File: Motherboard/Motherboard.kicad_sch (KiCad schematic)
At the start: 61 parts, among them J1 ATX-20, J2 65SIB_Connector, J3 DB9_Header, J4 GPIO_Connector, J5 Expansion_Connector, J6 Expansion_Connector, J7 Expansion_Connector, J8 Expansion_Connector, J9 Expansion_Connector, SW1 SW_SPST, U2 AS6C4008-55PCN, U3 ATF22V10C, U4 DS1813, U6 28C010, X1 ACO-8MHz

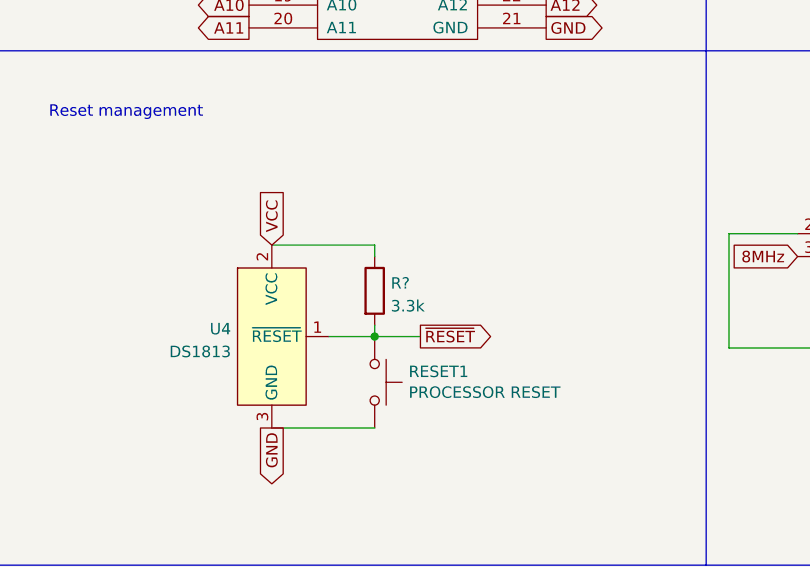
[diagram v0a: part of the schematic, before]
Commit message: 6 unrouted traces...
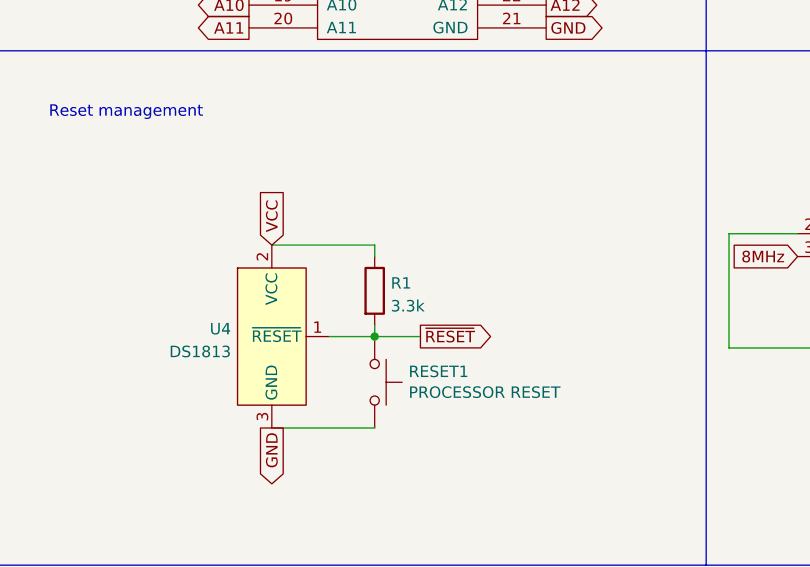
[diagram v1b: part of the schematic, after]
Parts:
- gave numbers to parts that had none: 1
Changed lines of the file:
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@@
   (symbol (lib_id "Device:R") (at 104.14 208.28 0) (unit 1)
     (in_bom yes) (on_board yes) (fields_autoplaced)
-    (property "Reference" "R?" (id 0) (at 105.918 207.4453 0)
+    (property "Reference" "R1" (id 0) (at 105.918 207.4453 0)
       (effects (font (size 1.27 1.27)) (justify left))
     )
@@
       (reference "PWR_OK1") (unit 1) (value "LED") (footprint "LED_THT:LED_D5.0mm")
     )
+    (path "/dde2964d-78c7-464b-aee8-feca4368665c"
+      (reference "R1") (unit 1) (value "3.3k") (footprint "")
+    )
     (path "/dcd42140-1abc-4c79-b38e-d454cf8ccfb6"
       (reference "R9") (unit 1) (value "220 Ω") (footprint "Resistor_THT:R_Axial_DIN0207_L6.3mm_D2.5mm_P7.62mm_Horizontal")
@@
       (reference "R21") (unit 1) (value "3.3k Ω") (footprint "Resistor_THT:R_Axial_DIN0207_L6.3mm_D2.5mm_P7.62mm_Horizontal")
     )
-    (path "/dde2964d-78c7-464b-aee8-feca4368665c"
-      (reference "R?") (unit 1) (value "3.3k") (footprint "")
-    )
     (path "/00000000-0000-0000-0000-00006196bac3"

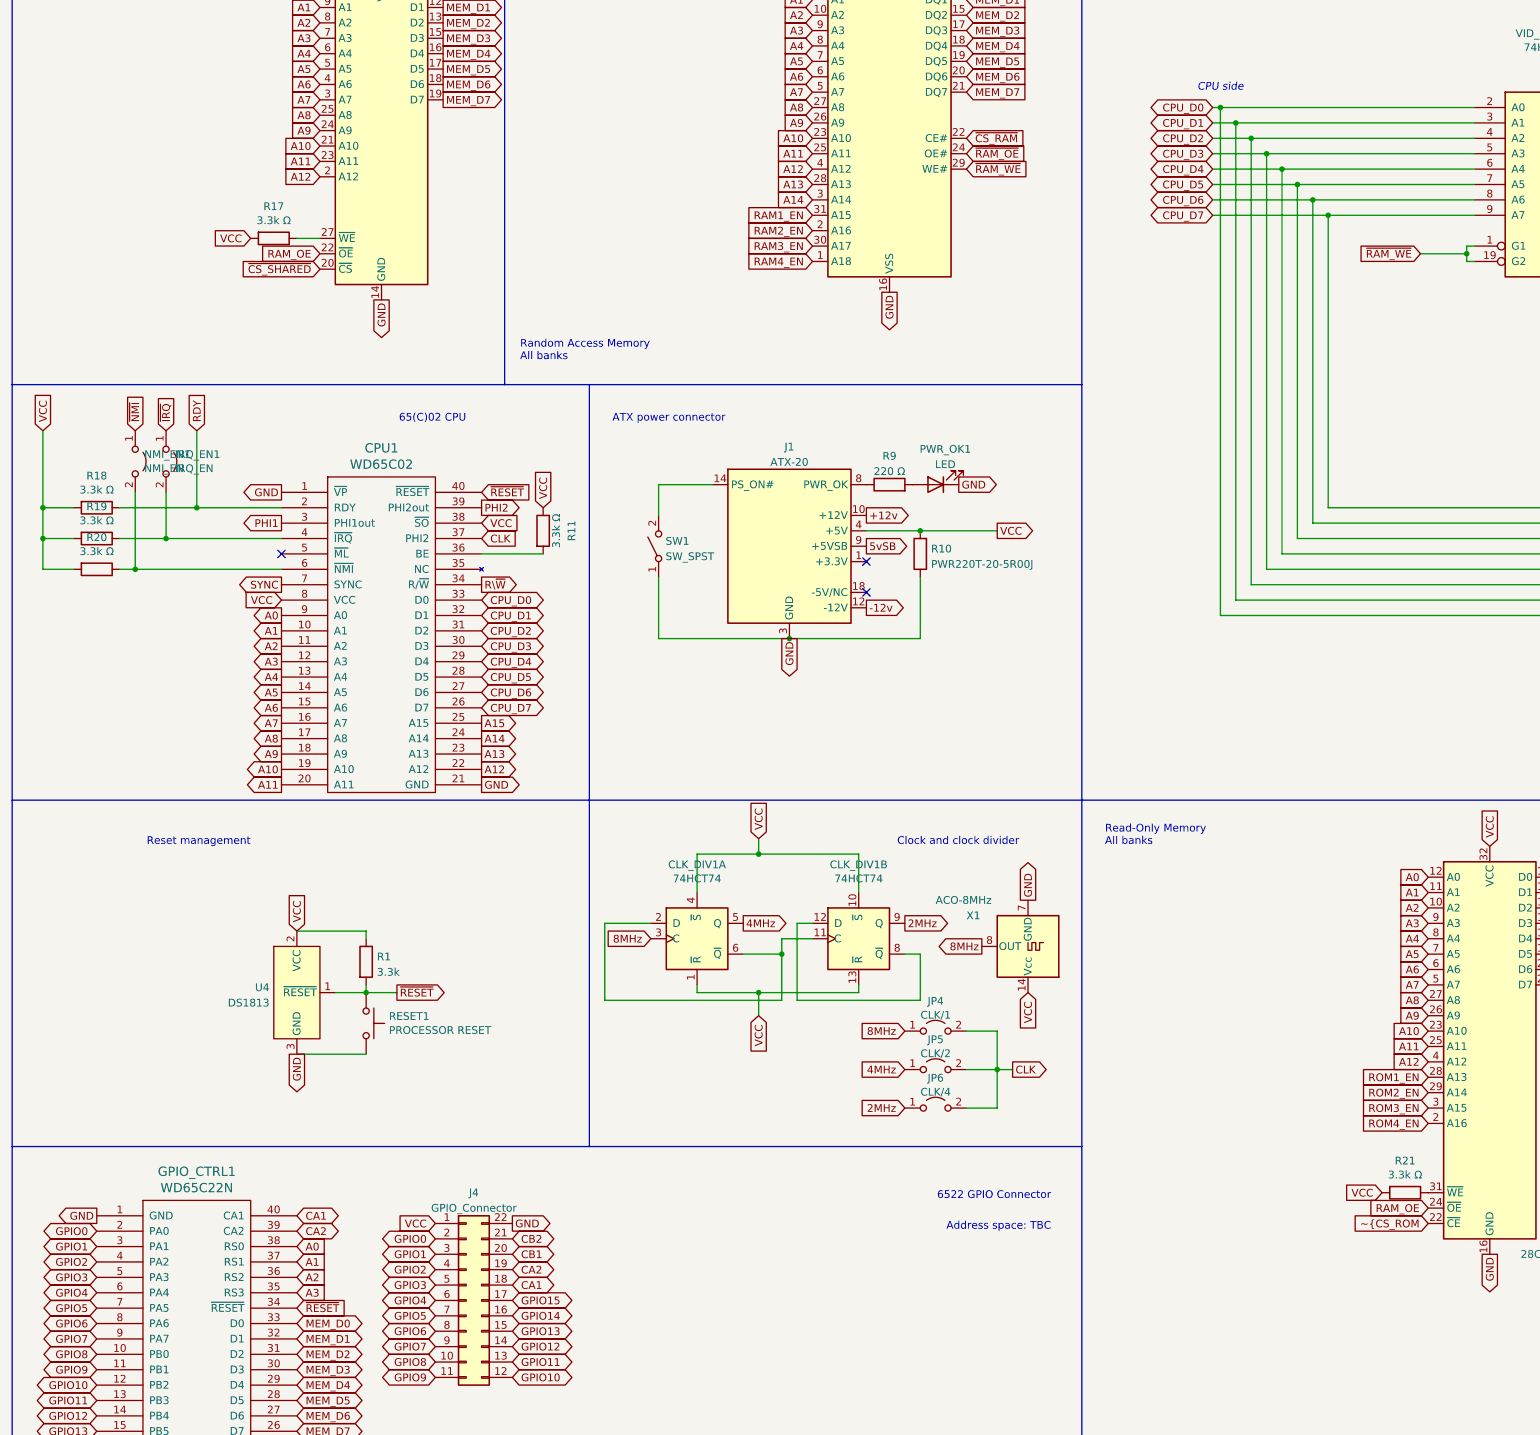
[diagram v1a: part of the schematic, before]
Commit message: Update Motherboard.kicad_sch
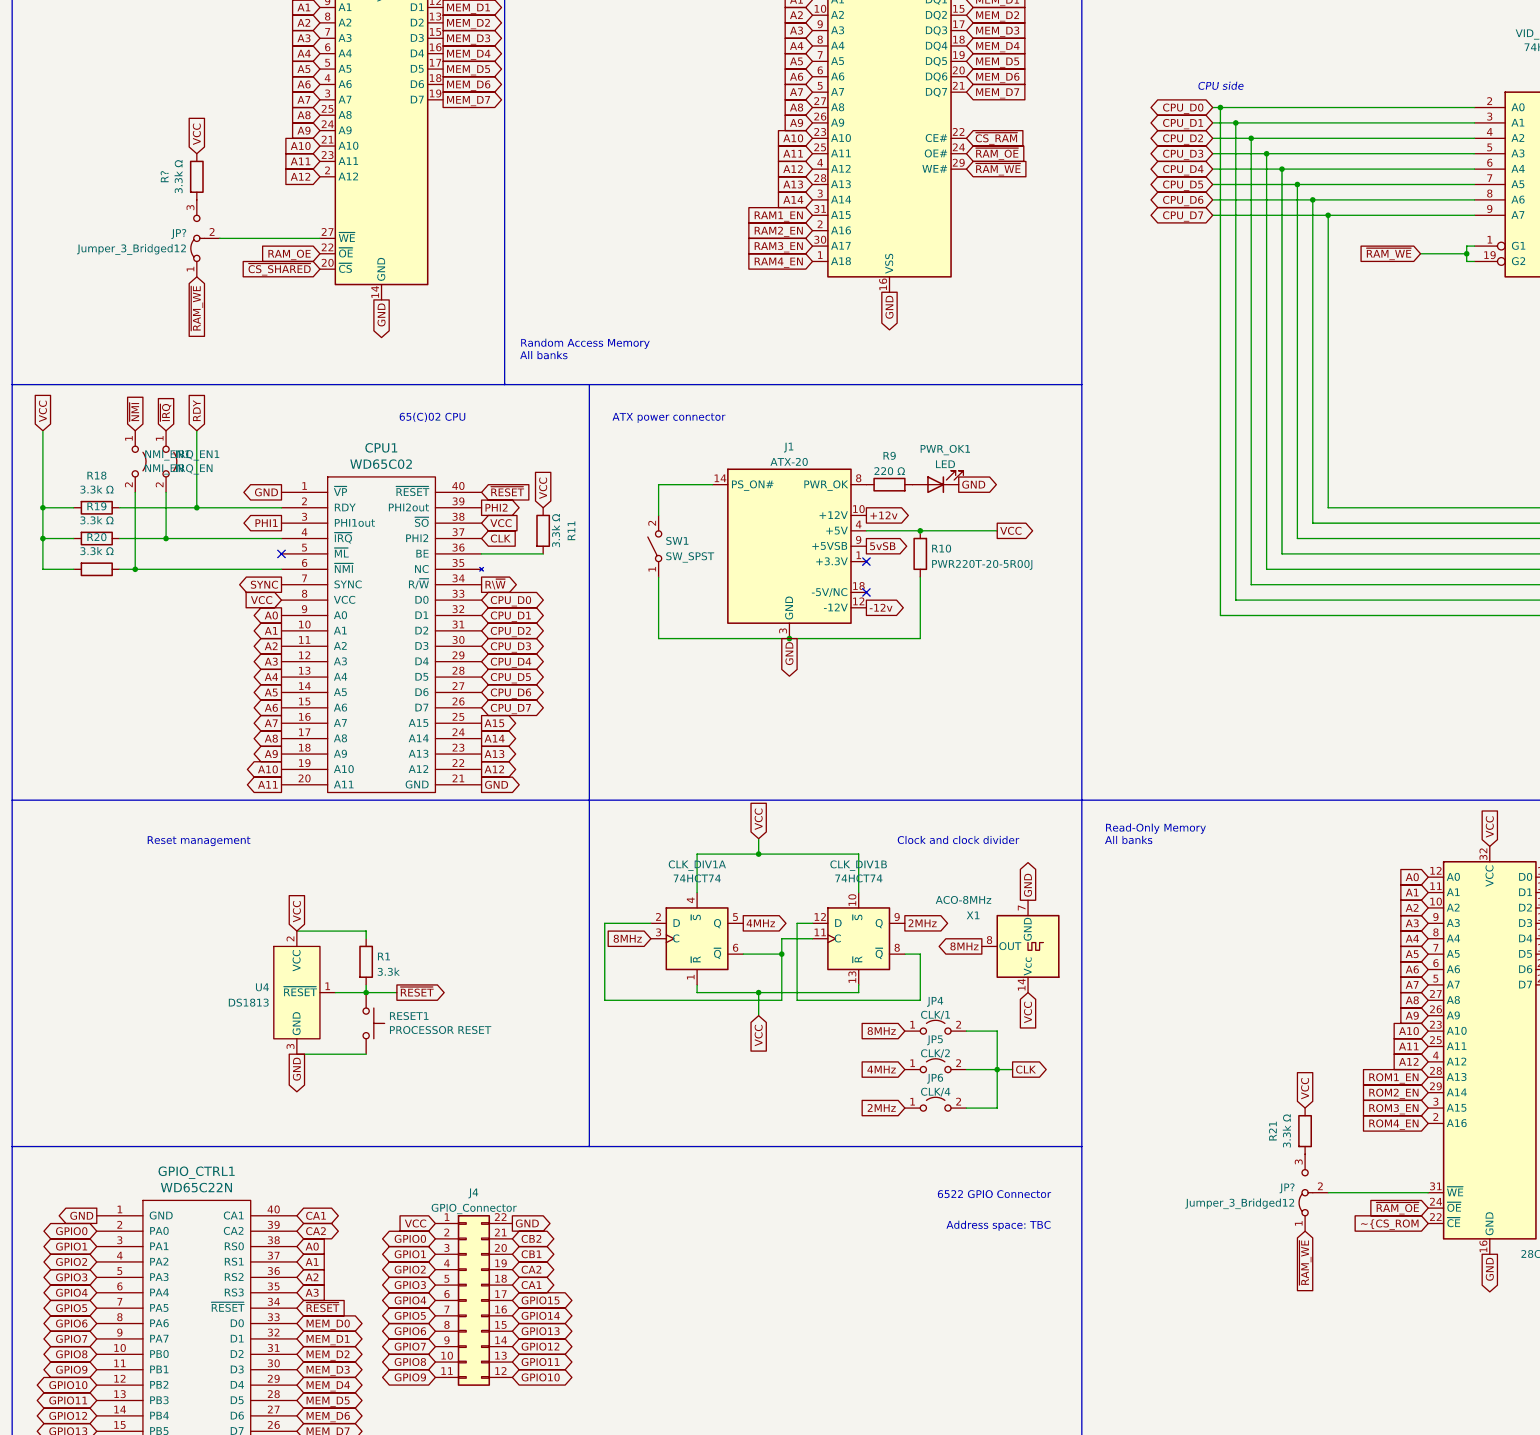
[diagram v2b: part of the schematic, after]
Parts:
- removed R17: 3.3k Ω, Resistor_THT:R_Axial_DIN0207_L6.3mm_D2.5mm_P7.62mm_Horizontal, symbol Device:R
- added JP? (x2): Jumper_3_Bridged12, symbol Jumper:Jumper_3_Bridged12
- added R?: 3.3k Ω, Resistor_THT:R_Axial_DIN0207_L6.3mm_D2.5mm_P7.62mm_Horizontal, symbol Device:R
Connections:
- net RAM_OE: no longer U6.24 (~{OE})
- net VCC: now also R21.1, R?.1; no longer R21.2
- net ~{RAM_OE}: now also U6.24 (~{OE})
- net ~{RAM_WE}: now also JP?.1 (A), JP?.1 (A)
- net at SHARED_ROM1.27 (~{WE}): now also JP?.2 (C)
- net at U6.31 (~{WE}): now also JP?.2 (C); no longer R21.1
- new net: JP?.3 (B), R21.2
- new net: JP?.3 (B), R?.2
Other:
- moved on the sheet: R21
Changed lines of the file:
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@@
     (stroke (width 0) (type default) (color 0 0 0 0))
   )
+  (wire (pts (xy 80.01 88.9) (xy 96.52 88.9))
+    (stroke (width 0) (type default) (color 0 0 0 0))
+  )
   (wire (pts (xy 349.25 72.39) (xy 355.6 72.39))
     (stroke (width 0) (type default) (color 0 0 0 0))
@@
     (stroke (width 0) (type default) (color 0 0 0 0))
   )
-  (wire (pts (xy 92.71 88.9) (xy 96.52 88.9))
-    (stroke (width 0) (type default) (color 0 0 0 0))
-  )
   (wire (pts (xy 158.75 190.5) (xy 168.91 190.5))
     (stroke (width 0) (type default) (color 0 0 0 0))
@@
     (stroke (width 0) (type default) (color 0 0 0 0))
   )
+  (wire (pts (xy 262.89 246.38) (xy 279.4 246.38))
+    (stroke (width 0) (type default) (color 0 0 0 0))
+  )
   (wire (pts (xy 243.84 72.39) (xy 250.19 72.39))
     (stroke (width 0) (type default) (color 0 0 0 0))
@@
     )
   )
+  (global_label "~{RAM_WE}" (shape input) (at 76.2 95.25 270) (fields_autoplaced)
+    (effects (font (size 1.27 1.27)) (justify right))
+    (property "Intersheet References" "${INTERSHEET_REFS}" (id 0) (at 76.1206 104.9523 90)
+      (effects (font (size 1.27 1.27)) (justify right) hide)
+    )
+  )
   (global_label "MEM_D2" (shape output) (at 116.84 53.34 0) (fields_autoplaced)
     (effects (font (size 1.27 1.27)) (justify left))
@@
     )
   )
+  (global_label "VCC" (shape input) (at 76.2 74.93 90) (fields_autoplaced)
+    (effects (font (size 1.27 1.27)) (justify left))
+    (property "Intersheet References" "${INTERSHEET_REFS}" (id 0) (at 311.15 -190.5 0)
+      (effects (font (size 1.27 1.27)) hide)
+    )
+  )
   (global_label "A11" (shape input) (at 751.84 322.58 180) (fields_autoplaced)
     (effects (font (size 1.27 1.27)) (justify right))
@@
     )
   )
-  (global_label "VCC" (shape input) (at 85.09 88.9 180) (fields_autoplaced)
-    (effects (font (size 1.27 1.27)) (justify right))
-    (property "Intersheet References" "${INTERSHEET_REFS}" (id 0) (at 0 0 0)
-      (effects (font (size 1.27 1.27)) hide)
-    )
-  )
   (global_label "~{RAM_OE}" (shape input) (at 203.2 74.93 0) (fields_autoplaced)
     (effects (font (size 1.27 1.27)) (justify left))
@@
     )
   )
+  (global_label "~{RAM_WE}" (shape input) (at 259.08 252.73 270) (fields_autoplaced)
+    (effects (font (size 1.27 1.27)) (justify right))
+    (property "Intersheet References" "${INTERSHEET_REFS}" (id 0) (at 259.0006 262.4323 90)
+      (effects (font (size 1.27 1.27)) (justify right) hide)
+    )
+  )
   (global_label "GPIO11" (shape bidirectional) (at 59.69 280.67 180) (fields_autoplaced)
     (effects (font (size 1.27 1.27)) (justify right))
@@
     )
   )
-  (global_label "RAM_OE" (shape input) (at 279.4 248.92 180) (fields_autoplaced)
+  (global_label "~{RAM_OE}" (shape input) (at 279.4 248.92 180) (fields_autoplaced)
     (effects (font (size 1.27 1.27)) (justify right))
     (property "Intersheet References" "${INTERSHEET_REFS}" (id 0) (at 269.8187 248.8406 0)
@@
     )
   )
-  (global_label "VCC" (shape input) (at 271.78 246.38 180) (fields_autoplaced)
-    (effects (font (size 1.27 1.27)) (justify right))
-    (property "Intersheet References" "${INTERSHEET_REFS}" (id 0) (at 6.35 11.43 0)
+  (global_label "VCC" (shape input) (at 259.08 232.41 90) (fields_autoplaced)
+    (effects (font (size 1.27 1.27)) (justify left))
+    (property "Intersheet References" "${INTERSHEET_REFS}" (id 0) (at 494.03 -33.02 0)
       (effects (font (size 1.27 1.27)) hide)
     )
@@
     )
   )
-  (symbol (lib_id "Device:R") (at 88.9 88.9 270) (unit 1)
-    (in_bom yes) (on_board yes)
-    (property "Reference" "R17" (id 0) (at 88.9 83.6422 90))
-    (property "Value" "3.3k Ω" (id 1) (at 88.9 85.9536 90))
-    (property "Footprint" "Resistor_THT:R_Axial_DIN0207_L6.3mm_D2.5mm_P7.62mm_Horizontal" (id 2) (at 88.9 87.122 90)
-      (effects (font (size 1.27 1.27)) hide)
-    )
-    (property "Datasheet" "~" (id 3) (at 88.9 88.9 0)
-      (effects (font (size 1.27 1.27)) hide)
-    )
-    (pin "1")
-    (pin "2")
-  )
   (symbol (lib_id "Device:R") (at 59.69 133.35 270) (unit 1)
     (in_bom yes) (on_board yes)
@@
     (pin "9")
   )
-  (symbol (lib_id "Device:R") (at 275.59 246.38 270) (unit 1)
+  (symbol (lib_id "Device:R") (at 259.08 236.22 0) (unit 1)
     (in_bom yes) (on_board yes)
-    (property "Reference" "R21" (id 0) (at 275.59 241.1222 90))
-    (property "Value" "3.3k Ω" (id 1) (at 275.59 243.4336 90))
-    (property "Footprint" "Resistor_THT:R_Axial_DIN0207_L6.3mm_D2.5mm_P7.62mm_Horizontal" (id 2) (at 275.59 244.602 90)
+    (property "Reference" "R21" (id 0) (at 253.8222 236.22 90))
+    (property "Value" "3.3k Ω" (id 1) (at 256.1336 236.22 90))
+    (property "Footprint" "Resistor_THT:R_Axial_DIN0207_L6.3mm_D2.5mm_P7.62mm_Horizontal" (id 2) (at 257.302 236.22 90)
       (effects (font (size 1.27 1.27)) hide)
     )
-    (property "Datasheet" "~" (id 3) (at 275.59 246.38 0)
+    (property "Datasheet" "~" (id 3) (at 259.08 236.22 0)
       (effects (font (size 1.27 1.27)) hide)
     )
@@
     (pin "7")
   )
+  (symbol (lib_id "Jumper:Jumper_3_Bridged12") (at 259.08 246.38 90) (unit 1)
+    (in_bom yes) (on_board yes) (fields_autoplaced)
+    (property "Reference" "JP?" (id 0) (at 257.4539 245.5453 90)
+      (effects (font (size 1.27 1.27)) (justify left))
+    )
+    (property "Value" "Jumper_3_Bridged12" (id 1) (at 257.4539 248.0822 90)
+      (effects (font (size 1.27 1.27)) (justify left))
+    )
+    (property "Footprint" "" (id 2) (at 259.08 246.38 0)
+      (effects (font (size 1.27 1.27)) hide)
+    )
+    (property "Datasheet" "~" (id 3) (at 259.08 246.38 0)
+      (effects (font (size 1.27 1.27)) hide)
+    )
+    (pin "1")
+    (pin "2")
+    (pin "3")
+  )
   (symbol (lib_id "Device:LED") (at 198.12 129.54 180) (unit 1)
     (in_bom yes) (on_board yes) (fields_autoplaced)
@@
     (pin "9")
   )
+  (symbol (lib_id "Jumper:Jumper_3_Bridged12") (at 76.2 88.9 90) (unit 1)
+    (in_bom yes) (on_board yes) (fields_autoplaced)
+    (property "Reference" "JP?" (id 0) (at 74.5739 88.0653 90)
+      (effects (font (size 1.27 1.27)) (justify left))
+    )
+    (property "Value" "Jumper_3_Bridged12" (id 1) (at 74.5739 90.6022 90)
+      (effects (font (size 1.27 1.27)) (justify left))
+    )
+    (property "Footprint" "" (id 2) (at 76.2 88.9 0)
+      (effects (font (size 1.27 1.27)) hide)
+    )
+    (property "Datasheet" "~" (id 3) (at 76.2 88.9 0)
+      (effects (font (size 1.27 1.27)) hide)
+    )
+    (pin "1")
+    (pin "2")
+    (pin "3")
+  )
   (symbol (lib_id "Device:R") (at 133.35 137.16 0) (unit 1)
     (in_bom yes) (on_board yes) (fields_autoplaced)
@@
     (pin "2")
   )
+  (symbol (lib_id "Device:R") (at 76.2 78.74 0) (unit 1)
+    (in_bom yes) (on_board yes)
+    (property "Reference" "R?" (id 0) (at 70.9422 78.74 90))
+    (property "Value" "3.3k Ω" (id 1) (at 73.2536 78.74 90))
+    (property "Footprint" "Resistor_THT:R_Axial_DIN0207_L6.3mm_D2.5mm_P7.62mm_Horizontal" (id 2) (at 74.422 78.74 90)
+      (effects (font (size 1.27 1.27)) hide)
+    )
+    (property "Datasheet" "~" (id 3) (at 76.2 78.74 0)
+      (effects (font (size 1.27 1.27)) hide)
+    )
+    (pin "1")
+    (pin "2")
+  )
   (symbol (lib_id "PC:Expansion_Connector") (at 720.09 312.42 0) (unit 1)
     (in_bom yes) (on_board yes)
@@
       (reference "JP6") (unit 1) (value "CLK/4") (footprint "Connector_PinHeader_2.54mm:PinHeader_1x02_P2.54mm_Vertical")
     )
+    (path "/6f4b6105-224e-42bf-b7e2-d653e1d8735d"
+      (reference "JP?") (unit 1) (value "Jumper_3_Bridged12") (footprint "")
+    )
+    (path "/add8bc41-e3d3-481e-b128-ae08b0cb09f3"
+      (reference "JP?") (unit 1) (value "Jumper_3_Bridged12") (footprint "")
+    )
     (path "/00000000-0000-0000-0000-000061a75d9b"
       (reference "NMI/IRQ1") (unit 1) (value "SW") (footprint "Connector_PinHeader_2.54mm:PinHeader_1x03_P2.54mm_Vertical")
@@
       (reference "R16") (unit 1) (value "3.3k Ω") (footprint "Resistor_THT:R_Axial_DIN0207_L6.3mm_D2.5mm_P7.62mm_Horizontal")
     )
-    (path "/00000000-0000-0000-0000-000061927174"
-      (reference "R17") (unit 1) (value "3.3k Ω") (footprint "Resistor_THT:R_Axial_DIN0207_L6.3mm_D2.5mm_P7.62mm_Horizontal")
-    )
     (path "/00000000-0000-0000-0000-000061928f59"
       (reference "R18") (unit 1) (value "3.3k Ω") (footprint "Resistor_THT:R_Axial_DIN0207_L6.3mm_D2.5mm_P7.62mm_Horizontal")
@@
       (reference "R21") (unit 1) (value "3.3k Ω") (footprint "Resistor_THT:R_Axial_DIN0207_L6.3mm_D2.5mm_P7.62mm_Horizontal")
     )
+    (path "/dff96944-e331-4220-a56d-d8c923ac86a8"
+      (reference "R?") (unit 1) (value "3.3k Ω") (footprint "Resistor_THT:R_Axial_DIN0207_L6.3mm_D2.5mm_P7.62mm_Horizontal")
+    )
     (path "/00000000-0000-0000-0000-00006196bac3"
